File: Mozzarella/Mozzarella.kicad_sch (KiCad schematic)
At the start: 6 parts, among them J1 RJ45_LED_Shielded_x2, U1 SeeeduinoXIAO

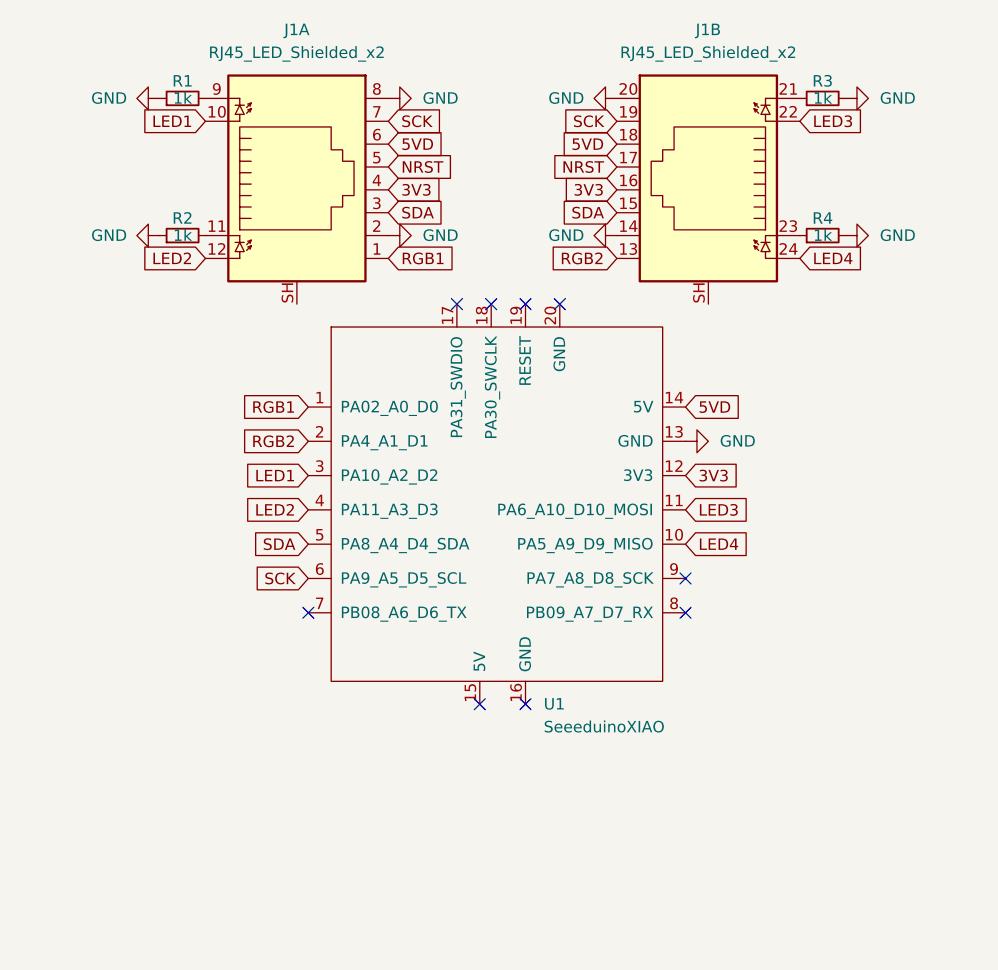
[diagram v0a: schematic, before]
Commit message: cleaned rj45 foot print
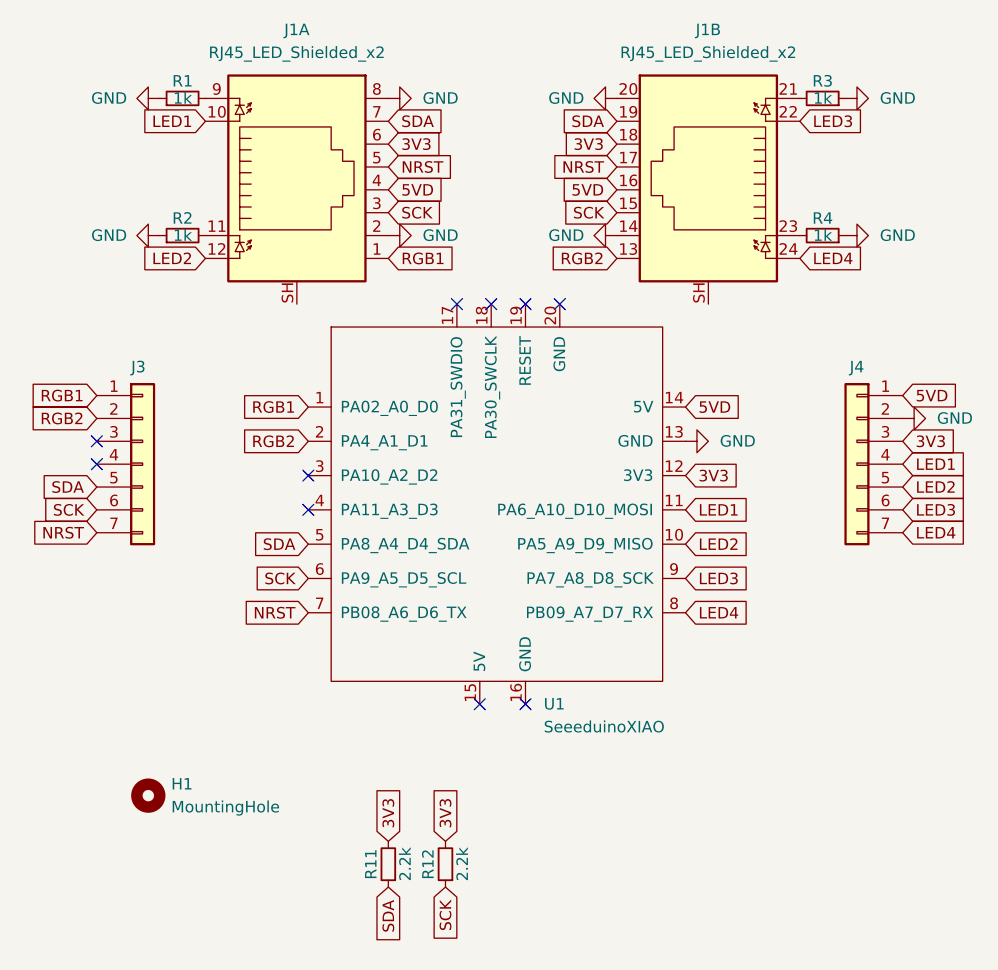
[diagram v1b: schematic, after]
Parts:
- added H1: MountingHole, MountingHole:MountingHole_2.2mm_M2, symbol Mechanical:MountingHole
- added J3, J4: Conn_01x07, 00_KeyParts:PinHeader_1x07_P2.54mm_Vertical, symbol Connector_Generic:Conn_01x07
- added R11, R12: 2.2k, 00_KeyParts:R_1608_HandSolder, symbol Device:R_Small
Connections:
- net 3V3: now also J1.18, J1.6, J4.3 (Pin_3), R11.2, R12.2; no longer J1.16, J1.4
- net 5VD: now also J1.16, J1.4, J4.1 (Pin_1); no longer J1.18, J1.6
- net GND: now also R3.1, R4.1, J4.2 (Pin_2); no longer R3.2, R4.2
- net LED1: now also U1.11 (PA6_A10_D10_MOSI), J4.4 (Pin_4); no longer U1.3 (PA10_A2_D2)
- net LED2: now also U1.10 (PA5_A9_D9_MISO), J4.5 (Pin_5); no longer U1.4 (PA11_A3_D3)
- net LED3: now also U1.9 (PA7_A8_D8_SCK), J4.6 (Pin_6); no longer U1.11 (PA6_A10_D10_MOSI)
- net LED4: now also U1.8 (PB09_A7_D7_RX), J4.7 (Pin_7); no longer U1.10 (PA5_A9_D9_MISO)
- net NRST: now also U1.7 (PB08_A6_D6_TX), J3.7 (Pin_7)
- net RGB1: now also J3.1 (Pin_1)
- net RGB2: now also J3.2 (Pin_2)
- net SCK: now also J1.15, J1.3, J3.6 (Pin_6), R12.1; no longer J1.19, J1.7
- net SDA: now also J1.19, J1.7, J3.5 (Pin_5), R11.1; no longer J1.15, J1.3
- net at J1.21: now also R3.2; no longer R3.1
- net at J1.23: now also R4.2; no longer R4.1
- no-connect marks 9 -> 10
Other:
- moved on the sheet: R3, R4

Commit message: rewiring
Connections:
- net GND: now also J1.SH, J1.SH
- net LED3: now also J4.7 (Pin_7), U1.8 (PB09_A7_D7_RX); no longer J4.6 (Pin_6), U1.9 (PA7_A8_D8_SCK)
- net LED4: now also J3.4 (Pin_4), U1.4 (PA11_A3_D3); no longer J4.7 (Pin_7), U1.8 (PB09_A7_D7_RX)
- net NRST: now also J3.3 (Pin_3), U1.3 (PA10_A2_D2); no longer J3.7 (Pin_7), U1.7 (PB08_A6_D6_TX)
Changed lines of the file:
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@@
 (kicad_sch (version 20211123) (generator eeschema)
   (paper "A4")
-  (no_connect (at 31.115 101.6))
+  (no_connect (at 31.115 111.76))
   (no_connect (at 71.12 86.36))
   (no_connect (at 82.55 86.36))
   (no_connect (at 73.66 130.81))
   (no_connect (at 78.74 86.36))
-  (no_connect (at 54.61 105.41))
-  (no_connect (at 54.61 109.22))
+  (no_connect (at 120.65 109.22))
   (no_connect (at 78.74 130.81))
-  (no_connect (at 31.115 104.14))
+  (no_connect (at 96.52 116.84))
+  (no_connect (at 54.61 120.65))
   (no_connect (at 74.93 86.36))
-  (global_label "LED3" (shape input) (at 96.52 116.84 0) (fields_autoplaced)
-    (effects (font (size 1.27 1.27)) (justify left))
-    (property "Intersheet References" "${INTERSHEET_REFS}" (id 0) (at 103.5898 116.7606 0)
+  (global_label "LED3" (shape input) (at 96.52 120.65 0) (fields_autoplaced)
+    (effects (font (size 1.27 1.27)) (justify left))
+    (property "Intersheet References" "${INTERSHEET_REFS}" (id 0) (at 103.5898 120.5706 0)
       (effects (font (size 1.27 1.27)) (justify left) hide)
     )
@@
     )
   )
-  (global_label "LED4" (shape input) (at 96.52 120.65 0) (fields_autoplaced)
-    (effects (font (size 1.27 1.27)) (justify left))
-    (property "Intersheet References" "${INTERSHEET_REFS}" (id 0) (at 103.5898 120.5706 0)
-      (effects (font (size 1.27 1.27)) (justify left) hide)
+  (global_label "LED4" (shape input) (at 54.61 109.22 180) (fields_autoplaced)
+    (effects (font (size 1.27 1.27)) (justify right))
+    (property "Intersheet References" "${INTERSHEET_REFS}" (id 0) (at 47.5402 109.2994 0)
+      (effects (font (size 1.27 1.27)) (justify right) hide)
     )
   )
@@
     )
   )
-  (global_label "NRST" (shape input) (at 31.115 111.76 180) (fields_autoplaced)
-    (effects (font (size 1.27 1.27)) (justify right))
-    (property "Intersheet References" "${INTERSHEET_REFS}" (id 0) (at 23.9243 111.8394 0)
+  (global_label "NRST" (shape input) (at 31.115 101.6 180) (fields_autoplaced)
+    (effects (font (size 1.27 1.27)) (justify right))
+    (property "Intersheet References" "${INTERSHEET_REFS}" (id 0) (at 23.9243 101.6794 0)
       (effects (font (size 1.27 1.27)) (justify right) hide)
     )
@@
     )
   )
-  (global_label "LED3" (shape input) (at 120.65 109.22 0) (fields_autoplaced)
-    (effects (font (size 1.27 1.27)) (justify left))
-    (property "Intersheet References" "${INTERSHEET_REFS}" (id 0) (at 127.7198 109.1406 0)
+  (global_label "LED3" (shape input) (at 120.65 111.76 0) (fields_autoplaced)
+    (effects (font (size 1.27 1.27)) (justify left))
+    (property "Intersheet References" "${INTERSHEET_REFS}" (id 0) (at 127.7198 111.6806 0)
       (effects (font (size 1.27 1.27)) (justify left) hide)
     )
@@
     )
   )
-  (global_label "NRST" (shape input) (at 54.61 120.65 180) (fields_autoplaced)
-    (effects (font (size 1.27 1.27)) (justify right))
-    (property "Intersheet References" "${INTERSHEET_REFS}" (id 0) (at 47.4193 120.7294 0)
+  (global_label "NRST" (shape input) (at 54.61 105.41 180) (fields_autoplaced)
+    (effects (font (size 1.27 1.27)) (justify right))
+    (property "Intersheet References" "${INTERSHEET_REFS}" (id 0) (at 47.4193 105.4894 0)
       (effects (font (size 1.27 1.27)) (justify right) hide)
     )
@@
     )
   )
-  (global_label "LED4" (shape input) (at 120.65 111.76 0) (fields_autoplaced)
-    (effects (font (size 1.27 1.27)) (justify left))
-    (property "Intersheet References" "${INTERSHEET_REFS}" (id 0) (at 127.7198 111.6806 0)
-      (effects (font (size 1.27 1.27)) (justify left) hide)
+  (global_label "LED4" (shape input) (at 31.115 104.14 180) (fields_autoplaced)
+    (effects (font (size 1.27 1.27)) (justify right))
+    (property "Intersheet References" "${INTERSHEET_REFS}" (id 0) (at 24.0452 104.2194 0)
+      (effects (font (size 1.27 1.27)) (justify right) hide)
     )
   )
@@
     (pin "6")
     (pin "7")
+  )
+  (symbol (lib_id "power:GND") (at 53.34 86.36 0) (unit 1)
+    (in_bom yes) (on_board yes)
+    (property "Reference" "#PWR0111" (id 0) (at 53.34 92.71 0)
+      (effects (font (size 1.27 1.27)) hide)
+    )
+    (property "Value" "GND" (id 1) (at 53.34 93.98 90)
+      (effects (font (size 1.27 1.27)) (justify left))
+    )
+    (property "Footprint" "" (id 2) (at 53.34 86.36 0)
+      (effects (font (size 1.27 1.27)) hide)
+    )
+    (property "Datasheet" "" (id 3) (at 53.34 86.36 0)
+      (effects (font (size 1.27 1.27)) hide)
+    )
+    (pin "1")
   )
   (symbol (lib_id "Device:R_Small") (at 69.85 148.59 180) (unit 1)
@@
     (pin "SH")
   )
+  (symbol (lib_id "power:GND") (at 99.06 86.36 0) (unit 1)
+    (in_bom yes) (on_board yes)
+    (property "Reference" "#PWR0112" (id 0) (at 99.06 92.71 0)
+      (effects (font (size 1.27 1.27)) hide)
+    )
+    (property "Value" "GND" (id 1) (at 99.06 93.98 90)
+      (effects (font (size 1.27 1.27)) (justify left))
+    )
+    (property "Footprint" "" (id 2) (at 99.06 86.36 0)
+      (effects (font (size 1.27 1.27)) hide)
+    )
+    (property "Datasheet" "" (id 3) (at 99.06 86.36 0)
+      (effects (font (size 1.27 1.27)) hide)
+    )
+    (pin "1")
+  )
   (symbol (lib_id "power:GND") (at 38.1 63.5 270) (unit 1)
     (in_bom yes) (on_board yes)
@@
       (reference "#PWR0110") (unit 1) (value "GND") (footprint "")
     )
+    (path "/2a288f14-115d-400d-a65e-5ebf9cd666a5"
+      (reference "#PWR0111") (unit 1) (value "GND") (footprint "")
+    )
+    (path "/e817a4b6-e5b7-47d8-9296-5b5e0ec191bb"
+      (reference "#PWR0112") (unit 1) (value "GND") (footprint "")
+    )
     (path "/9dbd817f-0427-4793-ad42-e0834f0f29ce"

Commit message: start wiring rella
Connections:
- net 3V3: now also R1.1, R2.1, R3.1, R4.1
- net GND: no longer R1.1, R2.1, R3.1, R4.1
- net LED1: now also J1.9; no longer J1.10
- net LED2: now also J1.11; no longer J1.12
- net LED3: now also J1.21; no longer J1.22
- net LED4: now also J1.23; no longer J1.24
- net at R2.2: now also J1.12; no longer J1.11
- net at R3.2: now also J1.22; no longer J1.21
- net at R1.2: now also J1.10; no longer J1.9
- net at R4.2: now also J1.24; no longer J1.23
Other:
- moved on the sheet: R1, R2, R3, R4
